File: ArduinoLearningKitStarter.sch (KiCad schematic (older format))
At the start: 80 parts, among them J1 USB_OTG, J2 CONN_01X08, J3 CONN_01X06, J4 CONN_01X08, J5 CONN_01X10, J6 CONN_01X04, J7 CONN_01X04, J8 CONN_01X02, SW1 SW_PUSH, SW2 SW_PUSH, SW3 SW_PUSH, U1 arduino_nano, U2 arduino_uno, U3 ESP32-DEVKIT-C

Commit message: Update schematic and board to KiCAD 5 (#37)
* Fix schematic libraries
* Update schematic and board to KiCAD 5
* Remove the rescue dir
* Update sheet info
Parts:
- C1, C2, C3: symbol C-RESCUE-robotarna_arduino -> Device:C
- C4, C5, C7, C8: value C_Small -> 10uF; symbol C_Small -> ArduinoLearningKitStarter:C_Small
- C6: value C_Small -> 10 μF; symbol C_Small -> ArduinoLearningKitStarter:C_Small
- DHT11: footprint Pin_Headers:Pin_Header_Straight_1x04 -> Connector_PinHeader_2.54mm:PinHeader_1x04_P2.54mm_Vertical; symbol CONN_01X04 -> ArduinoLearningKitStarter:Conn_01x04
- J1: symbol USB_OTG -> Connector:USB_B_Micro
- J2, J4: footprint yaqwsx:Pin_Header_Straight_1x08_circle -> Connector_PinHeader_2.54mm:PinHeader_1x08_P2.54mm_Vertical; symbol CONN_01X08 -> Connector_Generic:Conn_01x08
- J3: footprint yaqwsx:Pin_Header_Straight_1x06_circle -> Connector_PinHeader_2.54mm:PinHeader_1x06_P2.54mm_Vertical; symbol CONN_01X06 -> Connector_Generic:Conn_01x06
- J5: footprint yaqwsx:Pin_Header_Straight_1x10_circle -> Connector_PinHeader_2.54mm:PinHeader_1x10_P2.54mm_Vertical; symbol CONN_01X10 -> Connector_Generic:Conn_01x10
- J6: footprint Pin_Headers:Pin_Header_Straight_1x04 -> Connector_PinHeader_2.54mm:PinHeader_1x04_P2.54mm_Horizontal; symbol CONN_01X04 -> Connector_Generic:Conn_01x04
- J7: footprint Pin_Headers:Pin_Header_Straight_1x04 -> Connector_PinHeader_2.54mm:PinHeader_1x04_P2.54mm_Vertical; symbol CONN_01X04 -> Connector_Generic:Conn_01x04
- J8: footprint Pin_Headers:Pin_Header_Straight_1x02_Pitch2.54mm -> Connector_PinHeader_2.54mm:PinHeader_1x02_P2.54mm_Vertical; symbol CONN_01X02 -> Connector_Generic:Conn_01x02
- JP1, JP10, JP11, JP12, JP13, JP14, JP15, JP16, JP17, JP2, JP3, JP4, JP5, JP6, JP7, JP8, JP9: symbol Jumper_NC_Small -> Device:Jumper_NC_Small
- JP18: footprint (none) -> Connector_PinHeader_2.54mm:PinHeader_1x03_P2.54mm_Vertical; symbol Jumper_NC_Dual -> Device:Jumper_NC_Dual
- L_B1, L_G1, L_R1, L_Y1: footprint LEDs:LED-5MM -> LED_THT:LED_D5.0mm; symbol LED-RESCUE-robotarna_arduino -> Device:LED
- L_RGB1: footprint LEDs:LED-RGB-5MM_Common_Cathode -> LED_THT:LED_D5.0mm-4_RGB; symbol LED_RCBG-RESCUE-robotarna_arduino -> Device:LED_RCBG
- PHOTO1: symbol Photores -> Device:R_PHOTO
- PIEZO1: renamed from PIEIZO1; symbol PIEZO -> ArduinoLearningKitStarter:PIEZO-yaqwsx
- R1, R10, R11, R12, R13, R14, R15, R16, R17, R18, R19, R2, R20, R21, R22, R23, R24, R25, R3, R4, R5, R6, R7, R8, R9: symbol R-RESCUE-robotarna_arduino -> Device:R
- RV1, RV2: footprint Potentiometers:RV09 -> yaqwsx:RV09; symbol POT-RESCUE-robotarna_arduino -> Device:R_POT
- S1, S2, S3, S4, S5: footprint Pin_Headers:Pin_Header_Straight_1x03 -> Connector_PinHeader_2.54mm:PinHeader_1x03_P2.54mm_Vertical; symbol CONN_01X03 -> Connector_Generic:Conn_01x03
- SW1, SW2, SW3: footprint Buttons_Switches_ThroughHole:SW_PUSH_6mm -> Button_Switch_THT:SW_PUSH_6mm; symbol SW_PUSH -> Switch:SW_Push
- U1: symbol arduino_nano -> ArduinoLearningKitStarter:arduino_nano-yaqwsx
- U2: symbol arduino_uno -> ArduinoLearningKitStarter:arduino_uno-yaqwsx
- U3: symbol ESP32-DEVKIT-C -> ArduinoLearningKitStarter:ESP32-DEVKIT-C-yaqwsx
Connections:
- wire segments 91 -> 185

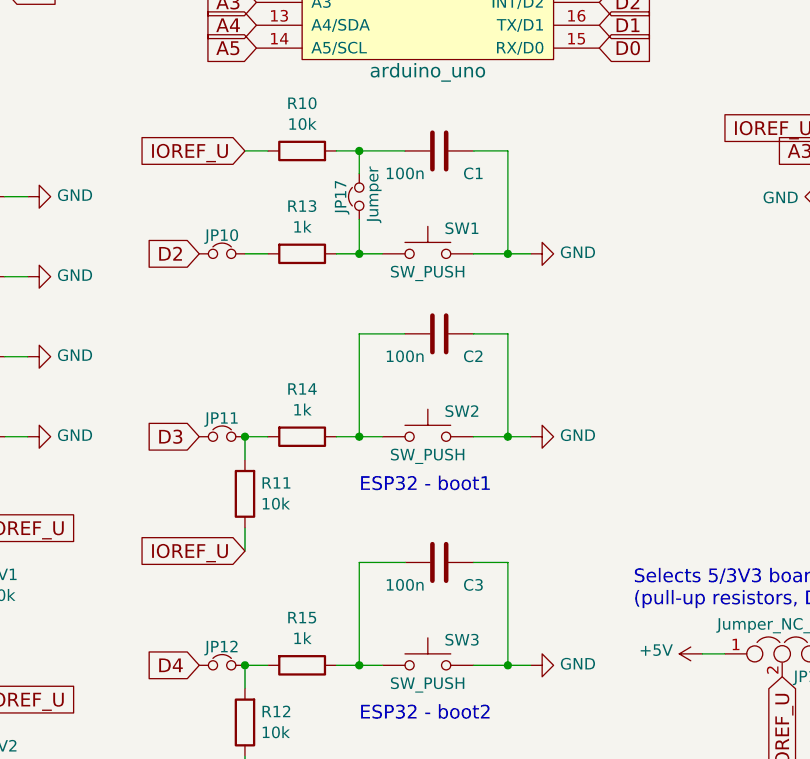
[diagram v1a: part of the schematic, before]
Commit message: Change values of blocking C (#26) and fix one unroute track
* Change values of capacitors C1, C2, C3 from 100 nF to 10 nF due to problems with flashing
ESP32 DevKitC.
* Fix unrouted GND track in left up corner (4th pad in second pinhead line from top of board).
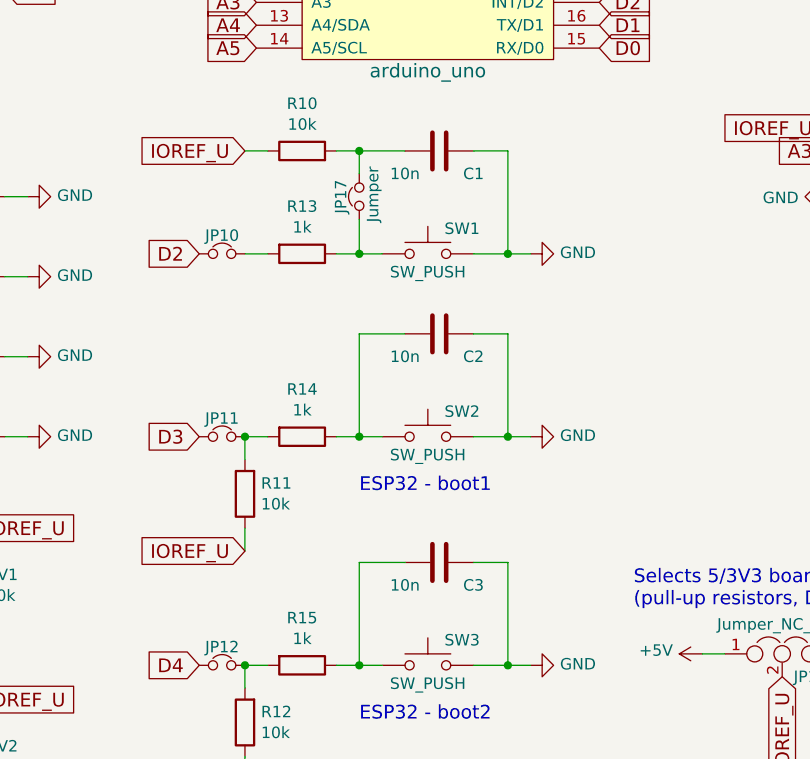
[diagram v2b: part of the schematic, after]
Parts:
- C1, C2, C3: value 100n -> 10n
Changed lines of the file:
@@
 Sheet 1 1
 Title "ArduinoLearningKitStarter"
-Date "2018-12-19"
-Rev "3.1"
+Date "2018-12-20"
+Rev "3.2"
 Comp "RoboticsBrno"
 Comment1 ""
@@
 P 8750 4850
 F 0 "C3" V 8850 5000 50  0000 C CNN
-F 1 "100n" V 8850 4700 50  0000 C CNN
+F 1 "10n" V 8850 4700 50  0000 C CNN
 F 2 "Capacitors_SMD:C_1206_HandSoldering" H 8750 4850 50  0001 C CNN
 F 3 "" H 8750 4850 50  0000 C CNN
@@
 P 8750 3050
 F 0 "C1" V 8850 3200 50  0000 C CNN
-F 1 "100n" V 8850 2900 50  0000 C CNN
+F 1 "10n" V 8850 2900 50  0000 C CNN
 F 2 "Capacitors_SMD:C_1206_HandSoldering" H 8750 3050 50  0001 C CNN
 F 3 "" H 8750 3050 50  0000 C CNN
@@
 P 8750 3850
 F 0 "C2" V 8850 4000 50  0000 C CNN
-F 1 "100n" V 8850 3700 50  0000 C CNN
+F 1 "10n" V 8850 3700 50  0000 C CNN
 F 2 "Capacitors_SMD:C_1206_HandSoldering" H 8750 3850 50  0001 C CNN
 F 3 "" H 8750 3850 50  0000 C CNN

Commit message: Suggest new layout
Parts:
- added H1, H2, H3, H4: Arduino Uno Mounting, MountingHole:MountingHole_2.2mm_M2, symbol Mechanical:MountingHole
- added H5, H6, H7, H8: Mounting Hole, MountingHole:MountingHole_2.2mm_M2, symbol Mechanical:MountingHole
- added J?: SPI, Connector_PinHeader_2.54mm:PinHeader_1x05_P2.54mm_Horizontal, symbol Connector_Generic:Conn_01x05
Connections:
- net D11: now also J?.3 (Pin_3)
- net D12: now also J?.2 (Pin_2)
- net D13: now also J?.1 (Pin_1)
- net GND: now also J?.5 (Pin_5)
- net IOREF_U: now also J?.4 (Pin_4)
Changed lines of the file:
@@
 Wire Wire Line
 	6050 3250 6150 3250
+$Comp
+L Mechanical:MountingHole H2
+U 1 1 5C1DAAED
+P 7050 6400
+F 0 "H2" H 7150 6446 50  0000 L CNN
+F 1 "Arduino Uno Mounting" H 7150 6355 50  0000 L CNN
+F 2 "MountingHole:MountingHole_2.2mm_M2" H 7050 6400 50  0001 C CNN
+F 3 "~" H 7050 6400 50  0001 C CNN
+	1    7050 6400
+	1    0    0    -1
+$EndComp
+$Comp
+L Mechanical:MountingHole H1
+U 1 1 5C1DB830
+P 7050 6200
+F 0 "H1" H 7150 6246 50  0000 L CNN
+F 1 "Arduino Uno Mounting" H 7150 6155 50  0000 L CNN
+F 2 "MountingHole:MountingHole_2.2mm_M2" H 7050 6200 50  0001 C CNN
+F 3 "~" H 7050 6200 50  0001 C CNN
+	1    7050 6200
+	1    0    0    -1
+$EndComp
+$Comp
+L Mechanical:MountingHole H3
+U 1 1 5C1DB922
+P 8100 6200
+F 0 "H3" H 8200 6246 50  0000 L CNN
+F 1 "Arduino Uno Mounting" H 8200 6155 50  0000 L CNN
+F 2 "MountingHole:MountingHole_2.2mm_M2" H 8100 6200 50  0001 C CNN
+F 3 "~" H 8100 6200 50  0001 C CNN
+	1    8100 6200
+	1    0    0    -1
+$EndComp
+$Comp
+L Mechanical:MountingHole H4
+U 1 1 5C1DBA12
+P 8100 6400
+F 0 "H4" H 8200 6446 50  0000 L CNN
+F 1 "Arduino Uno Mounting" H 8200 6355 50  0000 L CNN
+F 2 "MountingHole:MountingHole_2.2mm_M2" H 8100 6400 50  0001 C CNN
+F 3 "~" H 8100 6400 50  0001 C CNN
+	1    8100 6400
+	1    0    0    -1
+$EndComp
+$Comp
+L Mechanical:MountingHole H5
+U 1 1 5C1E65A4
+P 9250 6150
+F 0 "H5" H 9350 6196 50  0000 L CNN
+F 1 "Mounting Hole" H 9350 6105 50  0000 L CNN
+F 2 "MountingHole:MountingHole_2.2mm_M2" H 9250 6150 50  0001 C CNN
+F 3 "~" H 9250 6150 50  0001 C CNN
+	1    9250 6150
+	1    0    0    -1
+$EndComp
+$Comp
+L Mechanical:MountingHole H6
+U 1 1 5C1E68AB
+P 9250 6400
+F 0 "H6" H 9350 6446 50  0000 L CNN
+F 1 "Mounting Hole" H 9350 6355 50  0000 L CNN
+F 2 "MountingHole:MountingHole_2.2mm_M2" H 9250 6400 50  0001 C CNN
+F 3 "~" H 9250 6400 50  0001 C CNN
+	1    9250 6400
+	1    0    0    -1
+$EndComp
+$Comp
+L Mechanical:MountingHole H7
+U 1 1 5C1E6975
+P 10000 6150
+F 0 "H7" H 10100 6196 50  0000 L CNN
+F 1 "Mounting Hole" H 10100 6105 50  0000 L CNN
+F 2 "MountingHole:MountingHole_2.2mm_M2" H 10000 6150 50  0001 C CNN
+F 3 "~" H 10000 6150 50  0001 C CNN
+	1    10000 6150
+	1    0    0    -1
+$EndComp
+$Comp
+L Mechanical:MountingHole H8
+U 1 1 5C1E6A5D
+P 10000 6400
+F 0 "H8" H 10100 6446 50  0000 L CNN
+F 1 "Mounting Hole" H 10100 6355 50  0000 L CNN
+F 2 "MountingHole:MountingHole_2.2mm_M2" H 10000 6400 50  0001 C CNN
+F 3 "~" H 10000 6400 50  0001 C CNN
+	1    10000 6400
+	1    0    0    -1
+$EndComp
+$Comp
+L Connector_Generic:Conn_01x05 J?
+U 1 1 5C1EA8A1
+P 10650 3700
+F 0 "J?" H 10730 3742 50  0000 L CNN
+F 1 "SPI" H 10730 3651 50  0000 L CNN
+F 2 "Connector_PinHeader_2.54mm:PinHeader_1x05_P2.54mm_Horizontal" H 10650 3700 50  0001 C CNN
+F 3 "~" H 10650 3700 50  0001 C CNN
+	1    10650 3700
+	1    0    0    -1
+$EndComp
+$Comp
+L ArduinoLearningKitStarter:GND #PWR?
+U 1 1 5C1EAB4C
+P 10450 3900
+F 0 "#PWR?" H 10450 3650 50  0001 C CNN
+F 1 "GND" V 10455 3772 50  0000 R CNN
+F 2 "" H 10450 3900 50  0000 C CNN
+F 3 "" H 10450 3900 50  0000 C CNN
+	1    10450 3900
+	0    1    1    0
+$EndComp
+Text GLabel 10450 3800 0    60   Input ~ 0
+IOREF_U
+Text GLabel 10450 3600 0    60   Input ~ 0
+D12
+Text GLabel 10450 3500 0    60   Input ~ 0
+D13
+Text GLabel 10450 3700 0    60   Input ~ 0
+D11
 $EndSCHEMATC

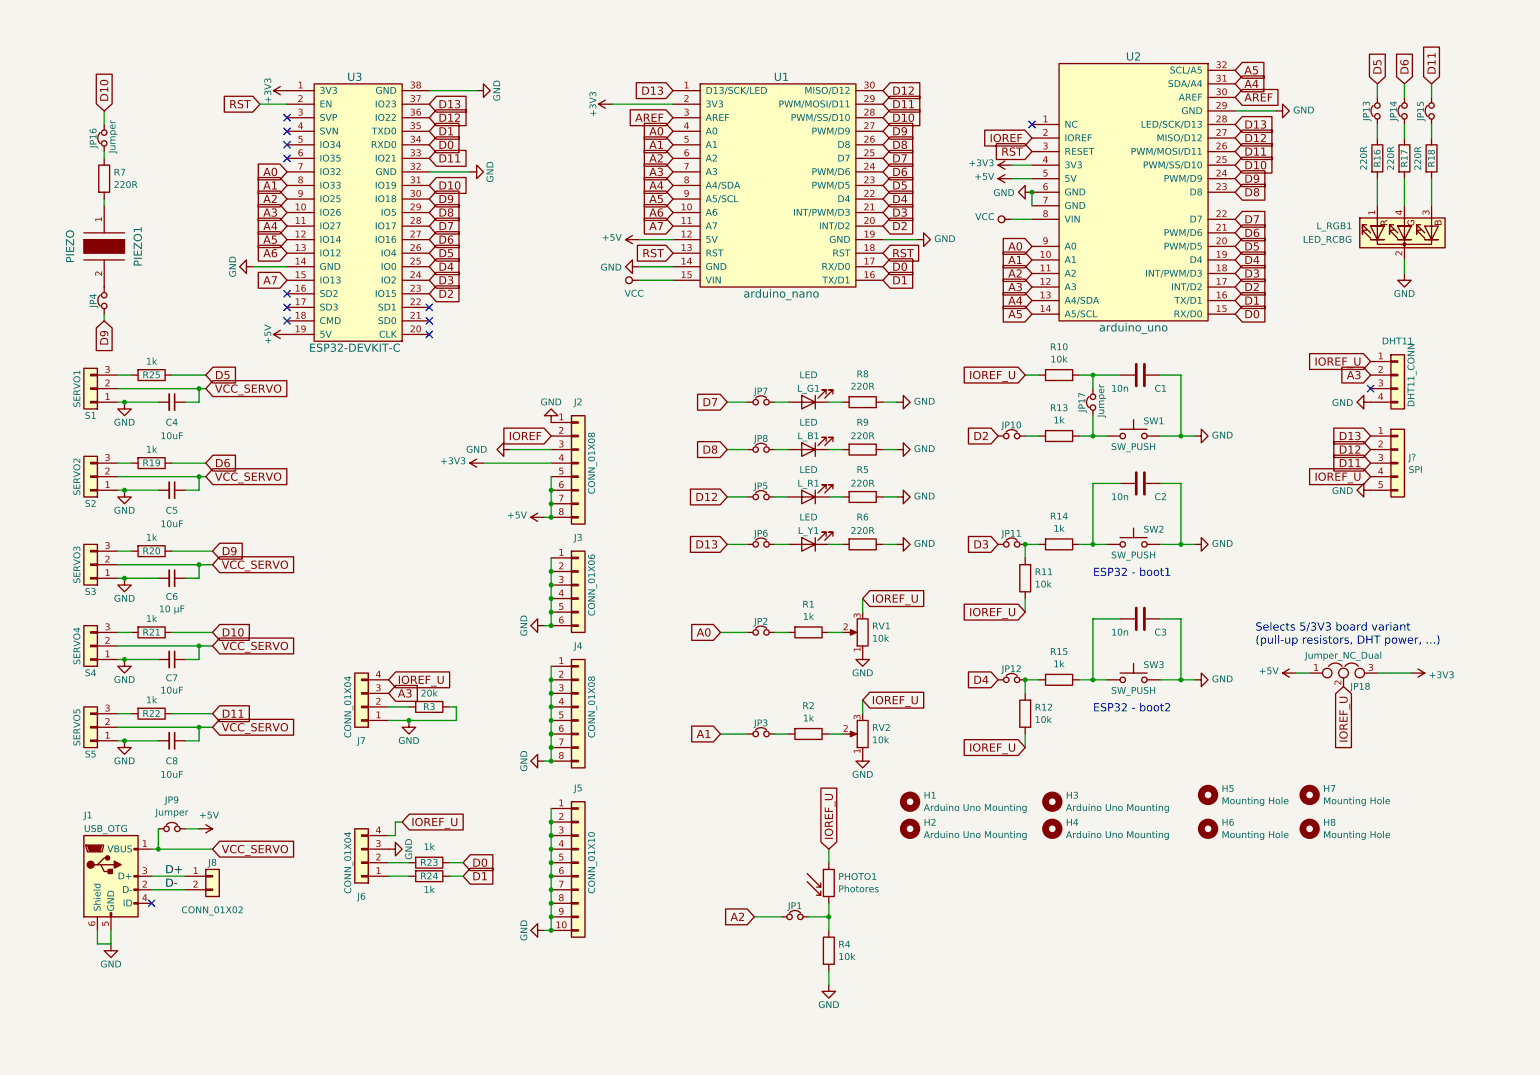
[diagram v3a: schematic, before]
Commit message: Add new labels
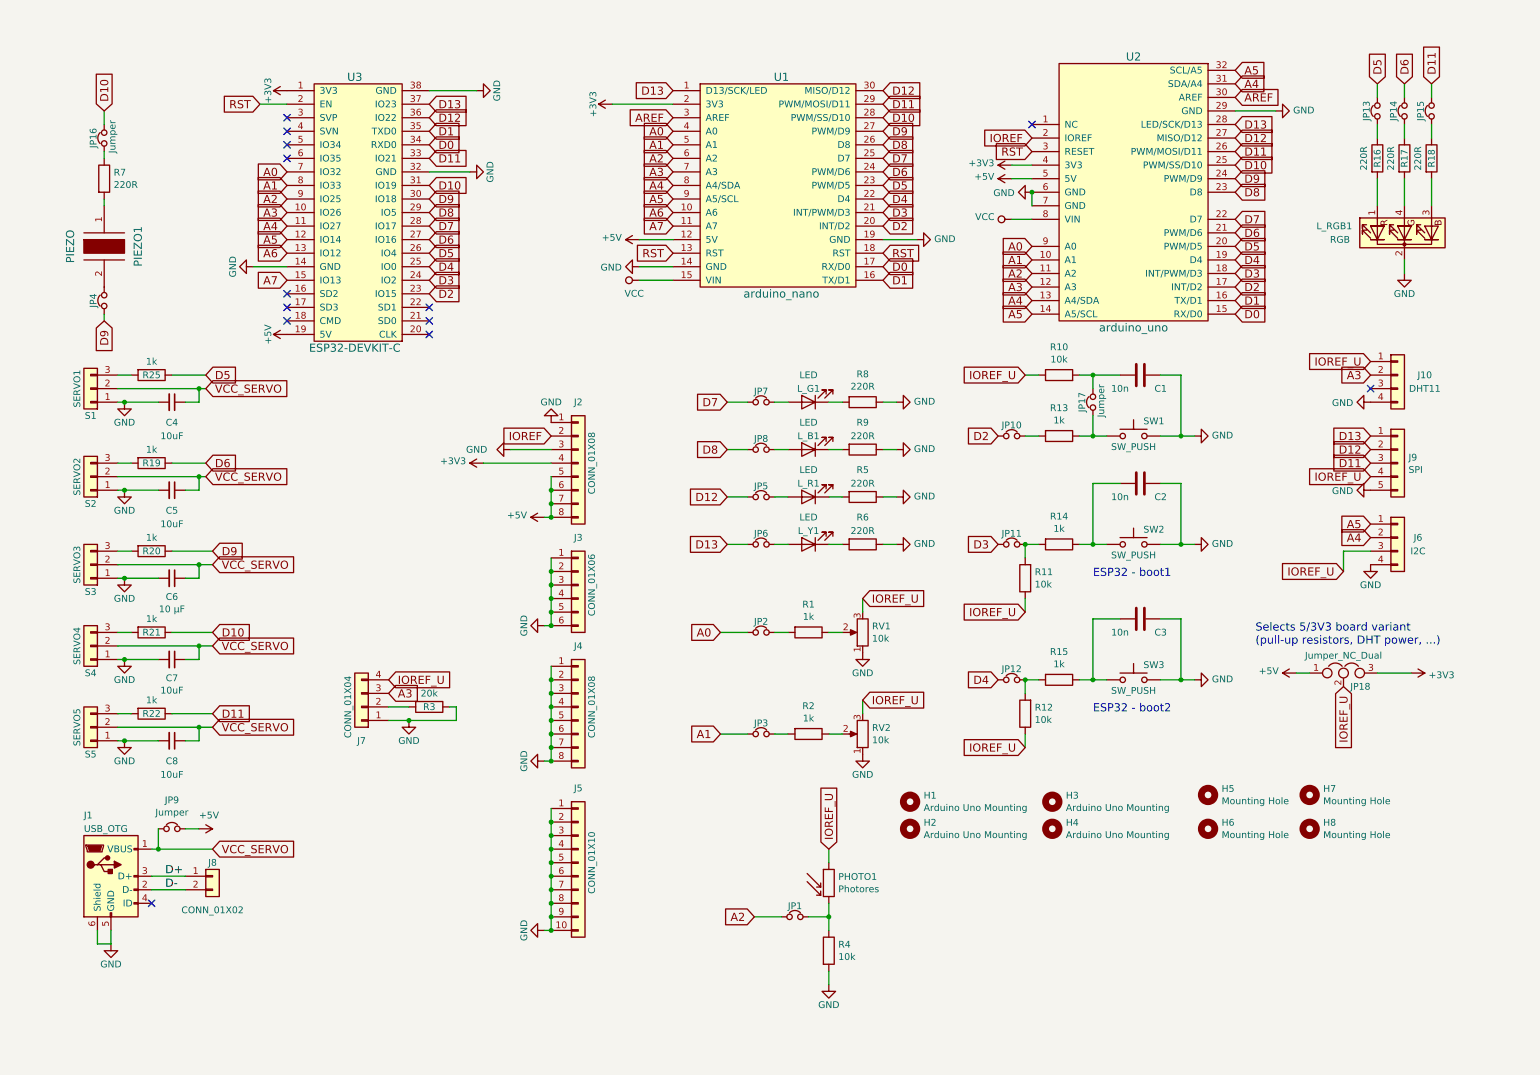
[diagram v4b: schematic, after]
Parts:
- removed R23, R24: 1k, Resistors_SMD:R_1206_HandSoldering, symbol Device:R
- J10: renamed from DHT11; value DHT11_CONN -> DHT11
- J6: value CONN_01X04 -> I2C; footprint Connector_PinHeader_2.54mm:PinHeader_1x04_P2.54mm_Horizontal -> ALKS:PinHeader_1x04_P2.54mm_Horizontal
- J9: renamed from J?; footprint Connector_PinHeader_2.54mm:PinHeader_1x05_P2.54mm_Horizontal -> ALKS:PinHeader_1x05_P2.54mm_Horizontal
- L_RGB1: value LED_RCBG -> RGB
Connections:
- net A4: now also J6.2 (Pin_2)
- net A5: now also J6.1 (Pin_1)
- net GND: now also J6.4 (Pin_4); no longer J6.3 (Pin_3)
- net IOREF_U: now also J6.3 (Pin_3); no longer J6.4 (Pin_4)
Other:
- moved on the sheet: J6
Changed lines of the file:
@@
 P 10700 2000
 F 0 "L_RGB1" V 10750 2650 50  0000 R CNN
-F 1 "LED_RCBG" V 10650 2750 50  0000 R CNN
+F 1 "RGB" V 10650 2550 50  0000 R CNN
 F 2 "LED_THT:LED_D5.0mm-4_RGB" H 10700 1950 50  0001 C CNN
 F 3 "" H 10700 1950 50  0000 C CNN
@@
 $EndComp
 $Comp
-L ArduinoLearningKitStarter:Conn_01x04 DHT11
+L ArduinoLearningKitStarter:Conn_01x04 J10
 U 1 1 57E4A74C
 P 10650 3050
-F 0 "DHT11" H 10650 3300 50  0000 C CNN
-F 1 "DHT11_CONN" V 10750 3050 50  0000 C CNN
+F 0 "J10" H 10850 3050 50  0000 C CNN
+F 1 "DHT11" H 10850 2950 50  0000 C CNN
 F 2 "Connector_PinHeader_2.54mm:PinHeader_1x04_P2.54mm_Vertical" H 10650 3050 50  0001 C CNN
 F 3 "" H 10650 3050 50  0000 C CNN
@@
 $EndComp
 $Comp
-L Device:R R23
-U 1 1 58C39409
-P 3500 6650
-F 0 "R23" V 3500 6650 50  0000 C CNN
-F 1 "1k" V 3384 6650 50  0000 C CNN
-F 2 "Resistors_SMD:R_1206_HandSoldering" H 3500 6650 50  0001 C CNN
-F 3 "" H 3500 6650 50  0001 C CNN
-	1    3500 6650
-	0    1    1    0
-$EndComp
-$Comp
-L Device:R R24
-U 1 1 58C39551
-P 3500 6750
-F 0 "R24" V 3500 6750 50  0000 C CNN
-F 1 "1k" V 3600 6750 50  0000 C CNN
-F 2 "Resistors_SMD:R_1206_HandSoldering" H 3500 6750 50  0001 C CNN
-F 3 "" H 3500 6750 50  0001 C CNN
-	1    3500 6750
-	0    1    1    0
-$EndComp
-$Comp
 L ArduinoLearningKitStarter:GND #PWR037
 U 1 1 58C39C30
-P 3200 6550
-F 0 "#PWR037" H 3200 6300 50  0001 C CNN
-F 1 "GND" H 3200 6400 50  0000 C CNN
-F 2 "" H 3200 6550 50  0000 C CNN
-F 3 "" H 3200 6550 50  0000 C CNN
-	1    3200 6550
-	0    -1   1    0
-$EndComp
-Text GLabel 3750 6750 2    60   Input ~ 0
-D1
+P 10450 4450
+F 0 "#PWR037" H 10450 4200 50  0001 C CNN
+F 1 "GND" H 10450 4300 50  0000 C CNN
+F 2 "" H 10450 4450 50  0000 C CNN
+F 3 "" H 10450 4450 50  0000 C CNN
+	1    10450 4450
+	-1   0    0    -1
+$EndComp
+Text GLabel 10450 4150 0    60   Input ~ 0
+A5
 $Comp
 L ArduinoLearningKitStarter:GND #PWR038
@@
 L Connector_Generic:Conn_01x04 J6
 U 1 1 58C39125
-P 3000 6650
-F 0 "J6" H 3000 6900 50  0000 C CNN
-F 1 "CONN_01X04" V 3100 6650 50  0000 C CNN
-F 2 "Connector_PinHeader_2.54mm:PinHeader_1x04_P2.54mm_Horizontal" H 3000 6650 50  0001 C CNN
-F 3 "" H 3000 6650 50  0001 C CNN
-	1    3000 6650
-	-1   0    0    1
+P 10650 4250
+F 0 "J6" H 10800 4250 50  0000 C CNN
+F 1 "I2C" H 10800 4150 50  0000 C CNN
+F 2 "ALKS:PinHeader_1x04_P2.54mm_Horizontal" H 10650 4250 50  0001 C CNN
+F 3 "" H 10650 4250 50  0001 C CNN
+	1    10650 4250
+	1    0    0    -1
 $EndComp
 Text GLabel 7900 4800 0    60   Input ~ 0
@@
 Text GLabel 6700 5450 2    60   Input ~ 0
 IOREF_U
-Text GLabel 3750 6650 2    60   Input ~ 0
-D0
+Text GLabel 10450 4250 0    60   Input ~ 0
+A4
 Text GLabel 3200 5300 2    60   Input ~ 0
 IOREF_U
-Text GLabel 3300 6350 2    60   Input ~ 0
+Text GLabel 10250 4500 0    60   Input ~ 0
 IOREF_U
 Text GLabel 10450 2950 0    60   Input ~ 0
@@
 	1300 5550 1200 5550
 Wire Wire Line
-	3650 6650 3750 6650
-Wire Wire Line
-	3650 6750 3750 6750
-Wire Wire Line
 	4400 4400 4400 4500
 Wire Wire Line
@@
 Wire Wire Line
 	9750 1100 9450 1100
-Wire Wire Line
-	3300 6350 3250 6350
-Wire Wire Line
-	3250 6350 3250 6450
-Wire Wire Line
-	3250 6450 3200 6450
-Wire Wire Line
-	3200 6650 3350 6650
-Wire Wire Line
-	3200 6750 3350 6750
 Wire Wire Line
 	1200 5750 1250 5750
@@
 $EndComp
 $Comp
-L Connector_Generic:Conn_01x05 J?
+L Connector_Generic:Conn_01x05 J9
 U 1 1 5C1EA8A1
 P 10650 3700
-F 0 "J?" H 10730 3742 50  0000 L CNN
+F 0 "J9" H 10730 3742 50  0000 L CNN
 F 1 "SPI" H 10730 3651 50  0000 L CNN
-F 2 "Connector_PinHeader_2.54mm:PinHeader_1x05_P2.54mm_Horizontal" H 10650 3700 50  0001 C CNN
+F 2 "ALKS:PinHeader_1x05_P2.54mm_Horizontal" H 10650 3700 50  0001 C CNN
 F 3 "~" H 10650 3700 50  0001 C CNN
 	1    10650 3700
@@
 $EndComp
 $Comp
-L ArduinoLearningKitStarter:GND #PWR?
+L ArduinoLearningKitStarter:GND #PWR0101
 U 1 1 5C1EAB4C
 P 10450 3900
-F 0 "#PWR?" H 10450 3650 50  0001 C CNN
+F 0 "#PWR0101" H 10450 3650 50  0001 C CNN
 F 1 "GND" V 10455 3772 50  0000 R CNN
 F 2 "" H 10450 3900 50  0000 C CNN
@@
 Text GLabel 10450 3700 0    60   Input ~ 0
 D11
+Wire Wire Line
+	10250 4500 10250 4350
+Wire Wire Line
+	10250 4350 10450 4350
 $EndSCHEMATC
